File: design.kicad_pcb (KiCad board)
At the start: 2 copper layers, 28.5 x 12 mm, 5 parts, among them J1 USB_C_Receptacle, J2 Conn_01x05, U1 ATtiny1616-M

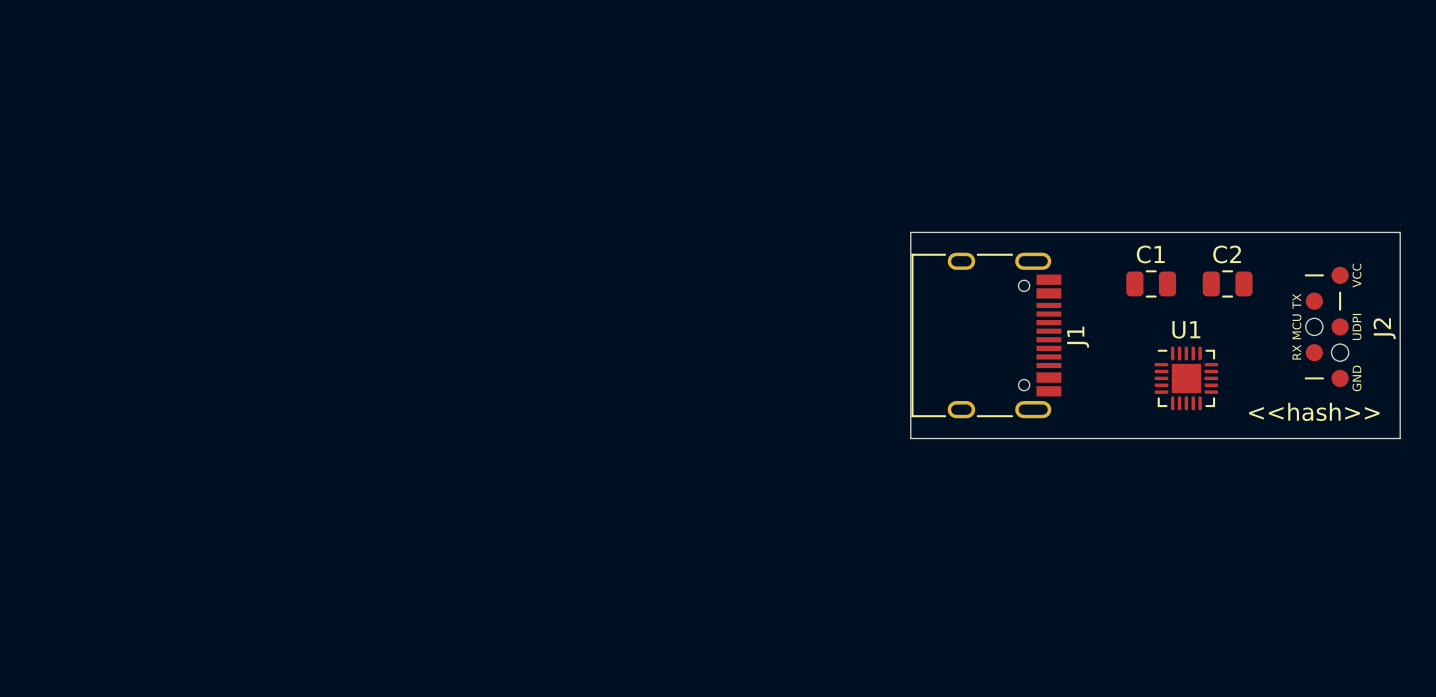
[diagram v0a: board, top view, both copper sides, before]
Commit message: PCB: placed components
and some cosmetic SCH stuff
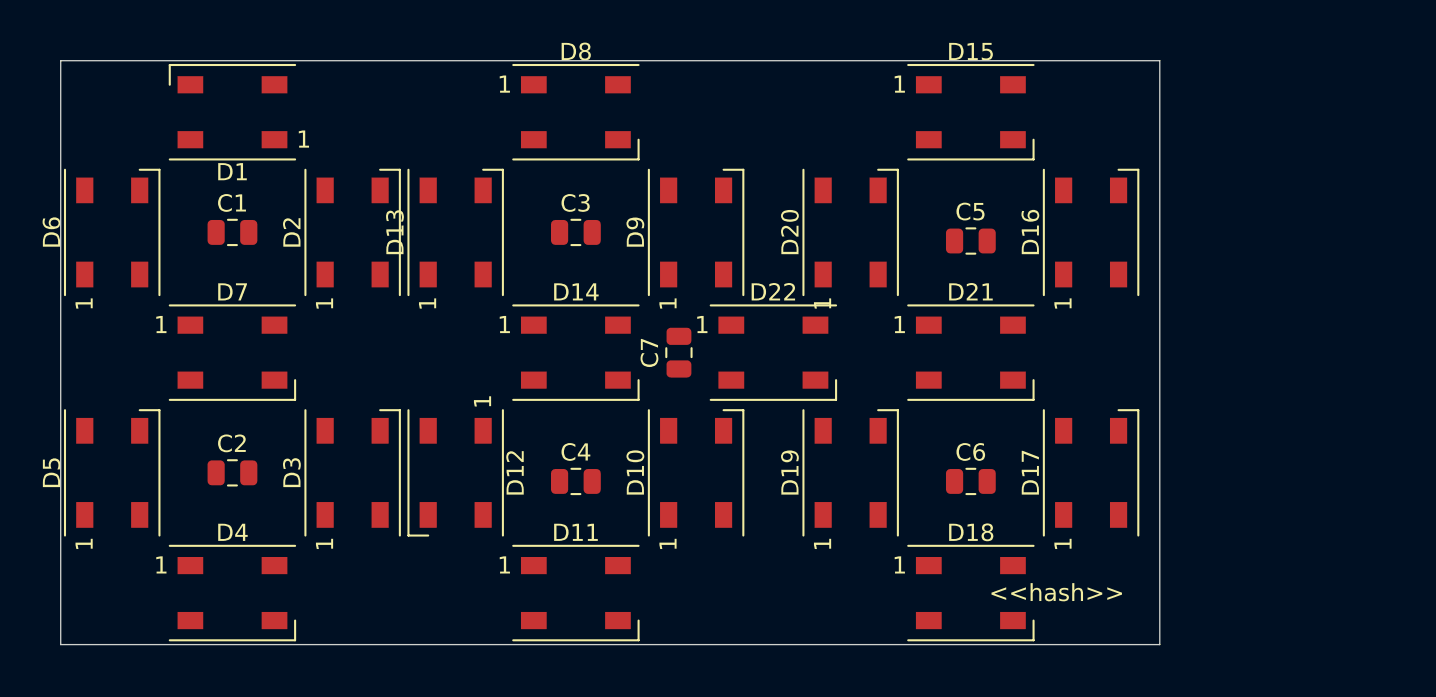
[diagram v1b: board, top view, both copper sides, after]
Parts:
- removed J1: USB_C_Receptacle, Connector_USB:USB_C_Receptacle_HRO_TYPE-C-31-M-12
- removed J2: Conn_01x05, E32-xxxT20D:UDPI_interface
- removed U1: ATtiny1616-M, Package_DFN_QFN:VQFN-20-1EP_3x3mm_P0.4mm_EP1.7x1.7mm
- added C3: 1uF, Capacitor_SMD:C_0805_2012Metric, F.Cu at (117.0, 80.0)
- added C4: 1uF, Capacitor_SMD:C_0805_2012Metric, F.Cu at (117.0, 94.5)
- added C5: 1uF, Capacitor_SMD:C_0805_2012Metric, F.Cu at (140.0, 80.5)
- added C6: 1uF, Capacitor_SMD:C_0805_2012Metric, F.Cu at (140.0, 94.5)
- added C7: 1uF, Capacitor_SMD:C_0805_2012Metric, F.Cu at (123.0, 87.0)
- added D1: WS2812B, LED_SMD:LED_WS2812B_PLCC4_5.0x5.0mm_P3.2mm, F.Cu at (97.0, 73.0)
- added D10: WS2812B, LED_SMD:LED_WS2812B_PLCC4_5.0x5.0mm_P3.2mm, F.Cu at (124.0, 94.0)
- added D11: WS2812B, LED_SMD:LED_WS2812B_PLCC4_5.0x5.0mm_P3.2mm, F.Cu at (117.0, 101.0)
- added D12: WS2812B, LED_SMD:LED_WS2812B_PLCC4_5.0x5.0mm_P3.2mm, F.Cu at (110.0, 94.0)
- added D13: WS2812B, LED_SMD:LED_WS2812B_PLCC4_5.0x5.0mm_P3.2mm, F.Cu at (110.0, 80.0)
- added D14: WS2812B, LED_SMD:LED_WS2812B_PLCC4_5.0x5.0mm_P3.2mm, F.Cu at (117.0, 87.0)
- added D15: WS2812B, LED_SMD:LED_WS2812B_PLCC4_5.0x5.0mm_P3.2mm, F.Cu at (140.0, 73.0)
- added D16: WS2812B, LED_SMD:LED_WS2812B_PLCC4_5.0x5.0mm_P3.2mm, F.Cu at (147.0, 80.0)
- added D17: WS2812B, LED_SMD:LED_WS2812B_PLCC4_5.0x5.0mm_P3.2mm, F.Cu at (147.0, 94.0)
- added D18: WS2812B, LED_SMD:LED_WS2812B_PLCC4_5.0x5.0mm_P3.2mm, F.Cu at (140.0, 101.0)
- added D19: WS2812B, LED_SMD:LED_WS2812B_PLCC4_5.0x5.0mm_P3.2mm, F.Cu at (133.0, 94.0)
- added D2: WS2812B, LED_SMD:LED_WS2812B_PLCC4_5.0x5.0mm_P3.2mm, F.Cu at (104.0, 80.0)
- added D20: WS2812B, LED_SMD:LED_WS2812B_PLCC4_5.0x5.0mm_P3.2mm, F.Cu at (133.0, 80.0)
- added D21: WS2812B, LED_SMD:LED_WS2812B_PLCC4_5.0x5.0mm_P3.2mm, F.Cu at (140.0, 87.0)
- added D22: WS2812B, LED_SMD:LED_WS2812B_PLCC4_5.0x5.0mm_P3.2mm, F.Cu at (128.5, 87.0)
- added D3: WS2812B, LED_SMD:LED_WS2812B_PLCC4_5.0x5.0mm_P3.2mm, F.Cu at (104.0, 94.0)
- added D4: WS2812B, LED_SMD:LED_WS2812B_PLCC4_5.0x5.0mm_P3.2mm, F.Cu at (97.0, 101.0)
- added D5: WS2812B, LED_SMD:LED_WS2812B_PLCC4_5.0x5.0mm_P3.2mm, F.Cu at (90.0, 94.0)
- added D6: WS2812B, LED_SMD:LED_WS2812B_PLCC4_5.0x5.0mm_P3.2mm, F.Cu at (90.0, 80.0)
- added D7: WS2812B, LED_SMD:LED_WS2812B_PLCC4_5.0x5.0mm_P3.2mm, F.Cu at (97.0, 87.0)
- added D8: WS2812B, LED_SMD:LED_WS2812B_PLCC4_5.0x5.0mm_P3.2mm, F.Cu at (117.0, 73.0)
- added D9: WS2812B, LED_SMD:LED_WS2812B_PLCC4_5.0x5.0mm_P3.2mm, F.Cu at (124.0, 80.0)
- C1, C2: value C_Small -> 1uF
- moved C2 59.0 mm to (97.0, 94.0)
- moved C1 53.6 mm to (97.0, 80.0)
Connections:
- C1 pad 1: Net-(C1-Pad1) -> VCC
- C1 pad 2: Net-(C1-Pad2) -> GND
- C2 pad 1: Net-(C2-Pad1) -> VCC
- C2 pad 2: Net-(C2-Pad2) -> GND
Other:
- board size 28.5 x 12 mm -> 64 x 34 mm

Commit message: SCH: annotation in the segment order
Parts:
- turned D5 to 270 degrees
- turned D6 to 270 degrees
- turned D7 to 180 degrees
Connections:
- D14 pad 2: Net-(D14-Pad2) -> Dmout
- D15 pad 2: Dmout -> Net-(D15-Pad2)
- D15 pad 4: Net-(D14-Pad2) -> Dmout
- D16 pad 4: Dmout -> Net-(D15-Pad2)
- D21 pad 2: Net-(D21-Pad2) -> Dmmout
- D22 pad 2: Dmmout -> Net-(D22-Pad2)
- D22 pad 4: Net-(D21-Pad2) -> Dmmout
- D8 pad 4: Dmmout -> Dhout
- D9 pad 4: Dhout -> Net-(D8-Pad2)

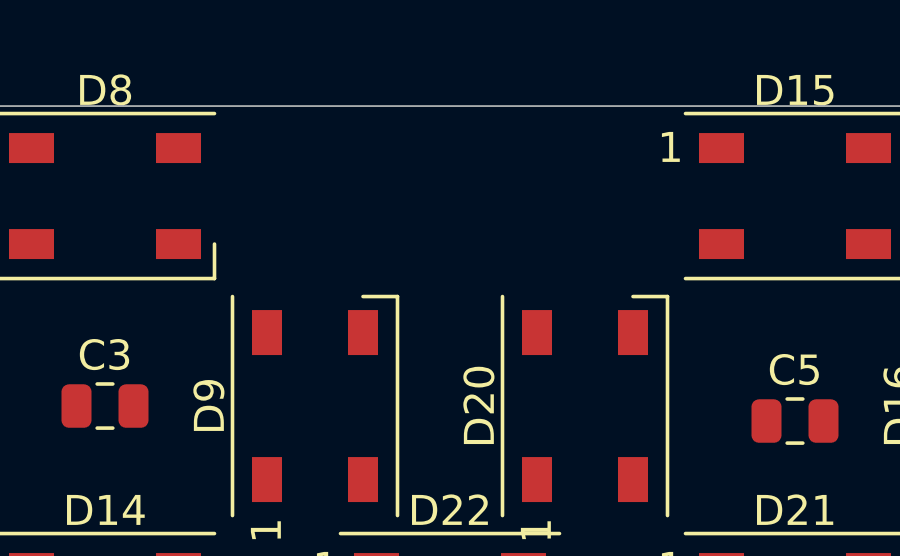
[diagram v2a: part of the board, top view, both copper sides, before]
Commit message: add pinheader footprint
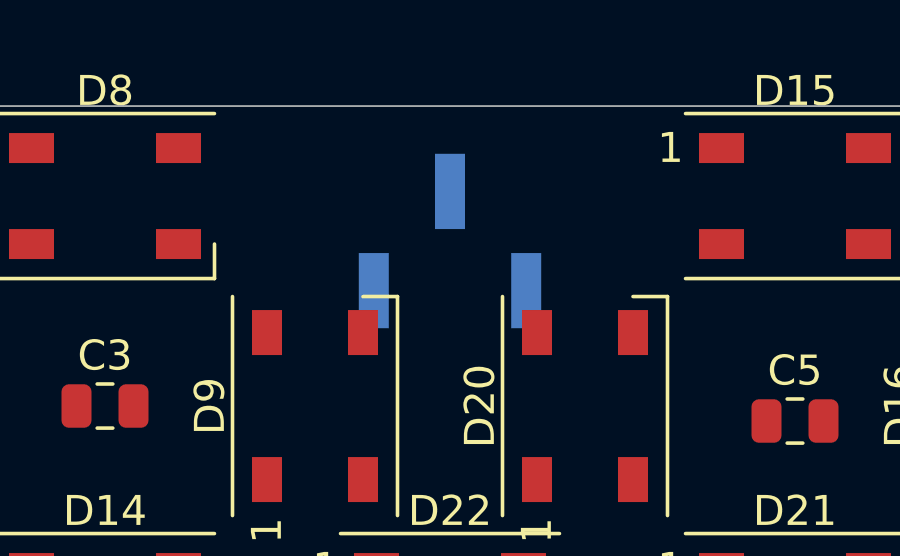
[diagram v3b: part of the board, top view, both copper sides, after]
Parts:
- added J1: Conn_01x03, Connector_PinHeader_2.54mm:PinHeader_1x03_P2.54mm_Vertical_SMD_Pin1Left, B.Cu at (128.5, 74.5)
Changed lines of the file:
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@@
     (tracks 0)
     (zones 0)
-    (modules 29)
+    (modules 30)
     (nets 26)
   )
@@
     (add_net VCC)
   )
+  (module Connector_PinHeader_2.54mm:PinHeader_1x03_P2.54mm_Vertical_SMD_Pin1Left (layer B.Cu)
+    (at 128.5 74.5 90)
+    (descr "surface-mounted straight pin header, 1x03, 2.54mm pitch, single row, style 1 (pin 1 left)")
+    (tags "Surface mounted pin header SMD 1x03 2.54mm single row style1 pin1 left")
+    (attr smd)
+    (fp_text reference J1 (at 0 4.87 90) (layer B.SilkS)
+      (effects (font (size 1 1) (thickness 0.15)) (justify mirror))
+    )
+    (fp_text value Conn_01x03 (at 0 -4.87 90) (layer B.Fab)
+      (effects (font (size 1 1) (thickness 0.15)) (justify mirror))
+    )
+    (fp_text user %R (at 0 0 180) (layer B.Fab)
+      (effects (font (size 1 1) (thickness 0.15)) (justify mirror))
+    )
+    (fp_line (start 1.27 -3.81) (end -1.27 -3.81) (layer B.Fab) (width 0.1))
+    (fp_line (start -0.32 3.81) (end 1.27 3.81) (layer B.Fab) (width 0.1))
+    (fp_line (start -1.27 -3.81) (end -1.27 2.86) (layer B.Fab) (width 0.1))
+    (fp_line (start -1.27 2.86) (end -0.32 3.81) (layer B.Fab) (width 0.1))
+    (fp_line (start 1.27 3.81) (end 1.27 -3.81) (layer B.Fab) (width 0.1))
+    (fp_line (start -1.27 2.86) (end -2.54 2.86) (layer B.Fab) (width 0.1))
+    (fp_line (start -2.54 2.86) (end -2.54 2.22) (layer B.Fab) (width 0.1))
+    (fp_line (start -2.54 2.22) (end -1.27 2.22) (layer B.Fab) (width 0.1))
+    (fp_line (start -1.27 -2.22) (end -2.54 -2.22) (layer B.Fab) (width 0.1))
+    (fp_line (start -2.54 -2.22) (end -2.54 -2.86) (layer B.Fab) (width 0.1))
+    (fp_line (start -2.54 -2.86) (end -1.27 -2.86) (layer B.Fab) (width 0.1))
+    (fp_line (start 1.27 0.32) (end 2.54 0.32) (layer B.Fab) (width 0.1))
+    (fp_line (start 2.54 0.32) (end 2.54 -0.32) (layer B.Fab) (width 0.1))
+    (fp_line (start 2.54 -0.32) (end 1.27 -0.32) (layer B.Fab) (width 0.1))
+    (fp_line (start -1.33 3.87) (end 1.33 3.87) (layer B.SilkS) (width 0.12))
+    (fp_line (start -1.33 -3.87) (end 1.33 -3.87) (layer B.SilkS) (width 0.12))
+    (fp_line (start 1.33 3.87) (end 1.33 0.76) (layer B.SilkS) (width 0.12))
+    (fp_line (start -1.33 3.3) (end -2.85 3.3) (layer B.SilkS) (width 0.12))
+    (fp_line (start -1.33 3.87) (end -1.33 3.3) (layer B.SilkS) (width 0.12))
+    (fp_line (start 1.33 -3.3) (end 1.33 -3.87) (layer B.SilkS) (width 0.12))
+    (fp_line (start 1.33 -0.76) (end 1.33 -3.87) (layer B.SilkS) (width 0.12))
+    (fp_line (start -1.33 1.78) (end -1.33 -1.78) (layer B.SilkS) (width 0.12))
+    (fp_line (start -3.45 4.35) (end -3.45 -4.35) (layer B.CrtYd) (width 0.05))
+    (fp_line (start -3.45 -4.35) (end 3.45 -4.35) (layer B.CrtYd) (width 0.05))
+    (fp_line (start 3.45 -4.35) (end 3.45 4.35) (layer B.CrtYd) (width 0.05))
+    (fp_line (start 3.45 4.35) (end -3.45 4.35) (layer B.CrtYd) (width 0.05))
+    (pad 2 smd rect (at 1.655 0 90) (size 2.51 1) (layers B.Cu B.Paste B.Mask)
+      (net 1 VCC))
+    (pad 3 smd rect (at -1.655 -2.54 90) (size 2.51 1) (layers B.Cu B.Paste B.Mask)
+      (net 4 GND))
+    (pad 1 smd rect (at -1.655 2.54 90) (size 2.51 1) (layers B.Cu B.Paste B.Mask)
+      (net 3 Din))
+    (model ${KISYS3DMOD}/Connector_PinHeader_2.54mm.3dshapes/PinHeader_1x03_P2.54mm_Vertical_SMD_Pin1Left.wrl
+      (at (xyz 0 0 0))
+      (scale (xyz 1 1 1))
+      (rotate (xyz 0 0 0))
+    )
+  )
   (module Capacitor_SMD:C_0805_2012Metric (layer F.Cu)

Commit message: PCB: change to 4 layer
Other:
- copper layers 2 -> 4
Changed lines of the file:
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@@
   (layers
     (0 F.Cu signal)
+    (1 In1.Cu power)
+    (2 In2.Cu power)
     (31 B.Cu signal)
     (32 B.Adhes user)
@@
     (45 Margin user)
     (46 B.CrtYd user)
-    (47 F.CrtYd user)
+    (47 F.CrtYd user hide)
     (48 B.Fab user)
-    (49 F.Fab user hide)
+    (49 F.Fab user)
   )
   (setup

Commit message: PCB: Layout Hour
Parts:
- moved J1 21.5 mm to (107.0, 75.5), turned to 270 degrees
- turned D8 to 180 degrees
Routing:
- net VCC: track 0.00 -> 42.3 mm, vias 0 -> 13
- net GND: track 0.00 -> 34.1 mm, vias 0 -> 13
- net Dhout: track 0.00 -> 22.0 mm
- net Net-(D6-Pad2): track 0.00 -> 13.7 mm
- net Din: track 0.00 -> 11.7 mm, vias 0 -> 1
- net Net-(D5-Pad2): track 0.00 -> 10.4 mm
- net Net-(D2-Pad2): track 0.00 -> 10.4 mm
- net Net-(D4-Pad2): track 0.00 -> 8.51 mm
- net Net-(D3-Pad2): track 0.00 -> 8.51 mm
- net Net-(D1-Pad2): track 0.00 -> 8.51 mm
- added copper zone on In1.Cu, net GND
- added copper zone on In2.Cu, net VCC

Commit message: PCB: mm layout
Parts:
- turned D13 to 270 degrees
- turned D14 to 180 degrees
- turned D15 to 180 degrees
- turned D19 to 270 degrees
- turned D20 to 270 degrees
- turned D21 to 180 degrees
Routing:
- net GND: track 34.1 -> 87.9 mm, vias 13 -> 29
- net VCC: track 42.3 -> 91.2 mm, vias 13 -> 27
- net Dmout: track 0.00 -> 24.6 mm
- net Net-(D20-Pad2): track 0.00 -> 14.6 mm
- net Net-(D13-Pad2): track 0.00 -> 14.1 mm
- net Dmmout: track 0.00 -> 11.5 mm, vias 0 -> 2
- net Net-(D10-Pad4): track 0.00 -> 10.5 mm
- net Net-(D16-Pad2): track 0.00 -> 10.4 mm
- net Net-(D19-Pad2): track 0.00 -> 10.4 mm
- net Net-(D12-Pad2): track 0.00 -> 10.4 mm
- net Net-(D15-Pad2): track 0.00 -> 8.63 mm
- net Net-(D18-Pad2): track 0.00 -> 8.46 mm
- net Net-(D10-Pad2): track 0.00 -> 8.34 mm
- net Net-(D17-Pad2): track 0.00 -> 8.28 mm
- net Net-(D11-Pad2): track 0.00 -> 8.22 mm
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
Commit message: PCB: Silkscreen
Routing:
- net VCC: track 91.2 -> 94.3 mm
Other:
- board text added: "Din"
- board text added: "GND"
- board text added: "VCC"
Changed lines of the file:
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@@
   (general
     (thickness 1.6)
-    (drawings 34)
-    (tracks 262)
+    (drawings 37)
+    (tracks 265)
     (zones 0)
     (modules 30)
@@
     (47 F.CrtYd user hide)
     (48 B.Fab user)
-    (49 F.Fab user)
+    (49 F.Fab user hide)
   )
   (setup
@@
     (tags capacitor)
     (attr smd)
-    (fp_text reference C1 (at 0 -1.68) (layer F.SilkS)
+    (fp_text reference C1 (at 0.6 -1.68) (layer F.SilkS)
       (effects (font (size 1 1) (thickness 0.15)))
     )
@@
     )
   )
+  (gr_text GND (at 109.6 80.5 90) (layer B.SilkS)
+    (effects (font (size 1 1) (thickness 0.15)) (justify mirror))
+  )
+  (gr_text VCC (at 107.1 80.5 90) (layer B.SilkS)
+    (effects (font (size 1 1) (thickness 0.15)) (justify mirror))
+  )
+  (gr_text Din (at 104.4 80.2 90) (layer B.SilkS)
+    (effects (font (size 1 1) (thickness 0.15)) (justify mirror))
+  )
   (gr_line (start 147 104) (end 147 70) (layer Dwgs.User) (width 0.15))
   (gr_line (start 133 104) (end 133 70) (layer Dwgs.User) (width 0.15))
@@
     (effects (font (size 1 1) (thickness 0.15)) (justify mirror))
   )
-  (via (at 101.5 74.5) (size 0.8) (drill 0.4) (layers F.Cu B.Cu) (net 1))
-  (segment (start 101.4 74.6) (end 101.5 74.5) (width 0.5) (layer F.Cu) (net 1))
-  (segment (start 99.45 74.6) (end 101.4 74.6) (width 0.5) (layer F.Cu) (net 1))
+  (via (at 97.1 74.6) (size 0.8) (drill 0.4) (layers F.Cu B.Cu) (net 1))
   (via (at 100 82) (size 0.8) (drill 0.4) (layers F.Cu B.Cu) (net 1))
-  (via (at 101 88) (size 0.8) (drill 0.4) (layers F.Cu B.Cu) (net 1))
-  (segment (start 100.4 88.6) (end 101 88) (width 0.5) (layer F.Cu) (net 1))
-  (segment (start 99.45 88.6) (end 100.4 88.6) (width 0.5) (layer F.Cu) (net 1))
+  (via (at 101.2 87.2) (size 0.8) (drill 0.4) (layers F.Cu B.Cu) (net 1))
   (segment (start 100.45 82.45) (end 100 82) (width 0.5) (layer F.Cu) (net 1))
   (segment (start 102.4 82.45) (end 100.45 82.45) (width 0.5) (layer F.Cu) (net 1))
@@
   (segment (start 118.1 76.6) (end 119.3 76.6) (width 0.5) (layer F.Cu) (net 1))
   (segment (start 116.05 78.65) (end 118.1 76.6) (width 0.5) (layer F.Cu) (net 1))
-  (via (at 122.4 84.4) (size 0.8) (drill 0.4) (layers F.Cu B.Cu) (net 1))
-  (segment (start 122.4 82.45) (end 122.4 84.4) (width 0.5) (layer F.Cu) (net 1))
-  (via (at 121.2 88.6) (size 0.8) (drill 0.4) (layers F.Cu B.Cu) (net 1))
-  (segment (start 119.45 88.6) (end 121.2 88.6) (width 0.5) (layer F.Cu) (net 1))
-  (segment (start 121.85 87.95) (end 121.2 88.6) (width 0.5) (layer F.Cu) (net 1))
-  (segment (start 123 87.95) (end 121.85 87.95) (width 0.5) (layer F.Cu) (net 1))
+  (via (at 123.8 80.9) (size 0.8) (drill 0.4) (layers F.Cu B.Cu) (net 1))
+  (via (at 122.1 89.5) (size 0.8) (drill 0.4) (layers F.Cu B.Cu) (net 1))
   (via (at 120.3 96.4) (size 0.8) (drill 0.4) (layers F.Cu B.Cu) (net 1))
   (segment (start 120.35 96.45) (end 120.3 96.4) (width 0.5) (layer F.Cu) (net 1))
@@
   (via (at 127.7 85.4) (size 0.8) (drill 0.4) (layers F.Cu B.Cu) (net 1))
   (segment (start 126.05 85.4) (end 127.7 85.4) (width 0.5) (layer F.Cu) (net 1))
-  (via (at 144.2 74.6) (size 0.8) (drill 0.4) (layers F.Cu B.Cu) (net 1))
-  (segment (start 142.45 74.6) (end 144.2 74.6) (width 0.5) (layer F.Cu) (net 1))
   (via (at 143.3 82.4) (size 0.8) (drill 0.4) (layers F.Cu B.Cu) (net 1))
   (segment (start 143.35 82.45) (end 143.3 82.4) (width 0.5) (layer F.Cu) (net 1))
@@
   (segment (start 143.05 96.45) (end 143 96.4) (width 0.5) (layer F.Cu) (net 1))
   (segment (start 145.4 96.45) (end 143.05 96.45) (width 0.5) (layer F.Cu) (net 1))
+  (segment (start 99.45 88.6) (end 99.45 87.85) (width 0.5) (layer F.Cu) (net 1))
+  (segment (start 100.1 87.2) (end 101.2 87.2) (width 0.5) (layer F.Cu) (net 1))
+  (segment (start 99.45 87.85) (end 100.1 87.2) (width 0.5) (layer F.Cu) (net 1))
+  (segment (start 99.45 74.6) (end 97.1 74.6) (width 0.5) (layer F.Cu) (net 1))
+  (segment (start 121.2 88.6) (end 122.1 89.5) (width 0.5) (layer F.Cu) (net 1))
+  (segment (start 119.45 88.6) (end 121.2 88.6) (width 0.5) (layer F.Cu) (net 1))
+  (segment (start 123 88.6) (end 122.1 89.5) (width 0.5) (layer F.Cu) (net 1))
+  (segment (start 123 87.95) (end 123 88.6) (width 0.5) (layer F.Cu) (net 1))
+  (segment (start 122.4 82.3) (end 123.8 80.9) (width 0.5) (layer F.Cu) (net 1))
+  (segment (start 122.4 82.45) (end 122.4 82.3) (width 0.5) (layer F.Cu) (net 1))
+  (via (at 142.5 76.9) (size 0.8) (drill 0.4) (layers F.Cu B.Cu) (net 1))
+  (segment (start 142.45 76.85) (end 142.5 76.9) (width 0.5) (layer F.Cu) (net 1))
+  (segment (start 142.45 74.6) (end 142.45 76.85) (width 0.5) (layer F.Cu) (net 1))
   (segment (start 99.45 71.4) (end 101.4 71.4) (width 0.25) (layer F.Cu) (net 2))
   (segment (start 102.4 72.4) (end 102.4 77.55) (width 0.25) (layer F.Cu) (net 2))
@@
   (via (at 125.6 75) (size 0.8) (drill 0.4) (layers F.Cu B.Cu) (net 4))
   (segment (start 125.6 77.55) (end 125.6 75) (width 0.5) (layer F.Cu) (net 4))
-  (via (at 121.2 86) (size 0.8) (drill 0.4) (layers F.Cu B.Cu) (net 4))
-  (segment (start 121.25 86.05) (end 121.2 86) (width 0.5) (layer F.Cu) (net 4))
-  (segment (start 123 86.05) (end 121.25 86.05) (width 0.5) (layer F.Cu) (net 4))
+  (via (at 121.2 85.3) (size 0.8) (drill 0.4) (layers F.Cu B.Cu) (net 4))
   (via (at 128.3 91.5) (size 0.8) (drill 0.4) (layers F.Cu B.Cu) (net 4))
   (segment (start 128.25 91.55) (end 128.3 91.5) (width 0.5) (layer F.Cu) (net 4))
@@
   (segment (start 108.4 83.6) (end 109.4 84.6) (width 0.5) (layer F.Cu) (net 4))
   (segment (start 108.4 82.45) (end 108.4 83.6) (width 0.5) (layer F.Cu) (net 4))
+  (segment (start 121.95 86.05) (end 121.2 85.3) (width 0.5) (layer F.Cu) (net 4))
+  (segment (start 123 86.05) (end 121.95 86.05) (width 0.5) (layer F.Cu) (net 4))
   (segment (start 105.6 82.45) (end 105.6 84.4) (width 0.25) (layer F.Cu) (net 5))
   (segment (start 102.4 87.6) (end 102.4 91.55) (width 0.25) (layer F.Cu) (net 5))
